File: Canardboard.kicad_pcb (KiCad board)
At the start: 4 copper layers, 56.1 x 68.5 mm, 143 parts, among them IC1 SIC437DED-T1-GE3, J1 RBUS, J2 USB_C_Receptacle_USB2.0, J3 Micro_SD_Card_Det, J4 Conn_01x02_Male, J5 Conn_01x03_Male, J6 Conn_01x03_Male, J7 Conn_01x03_Male, Q1 PXP012-30QLJ, Q10 PXP012-30QLJ, Q2 PXP012-30QLJ, Q3 PXP012-30QLJ, Q4 PXP012-30QLJ, Q5 PXP012-30QLJ, Q6 PXP012-30QLJ, Q7 PXP012-30QLJ, Q8 PXP012-30QLJ, Q9 PXP012-30QLJ, U1 ESP32-S3, U10 MP28167GQ-A-Z, U11 LTC4412xS6, U12 LTC4412xS6, U2 SN65HVD230, U3 LTC4412xS6, U4 LTC4412xS6, U5 LTC4412xS6, U7 ICM-20608-G, U8 MMC5983MA, Y1 40MHz±10ppm

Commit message: I don't want to lose all my changes so I will commit, commit.
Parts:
- removed C20: 390uF, Capacitor_SMD:CP_Elec_8x11.9
- removed C47: 100uF, Capacitor_SMD:CP_Elec_6.3x5.4
- removed Q10, Q3, Q5, Q7, Q8, Q9: PXP012-30QLJ, iclr:PXP01230QLJ
- removed U11, U12, U5: LTC4412xS6, Package_TO_SOT_SMD:TSOT-23-6
- added C18: 47uF, Capacitor_SMD:C_1206_3216Metric, F.Cu at (104.4, 84.1)
- added C19: 47uF, Capacitor_SMD:C_1206_3216Metric, F.Cu at (104.4, 81.6)
- added D3: D_Schottky, Diode_SMD:D_SOD-323, F.Cu at (109.0, 100.8)
- added D4: D_Schottky, Diode_SMD:D_SOD-323, F.Cu at (104.5, 122.9)
- added D5: D_Schottky, Diode_SMD:D_SOD-323, F.Cu at (110.6, 90.5)
- added R14: 10k, Resistor_SMD:R_0402_1005Metric, F.Cu at (128.5, 92.2)
- added TP10: TestPoint, TestPoint:TestPoint_Pad_D1.0mm, F.Cu at (122.8, 90.4)
- added TP11: TestPoint, TestPoint:TestPoint_Pad_D1.0mm, F.Cu at (126.0, 90.0)
- added TP12: TestPoint, TestPoint:TestPoint_Pad_D1.0mm, F.Cu at (128.1, 90.0)
- added TP13: TestPoint, TestPoint:TestPoint_Pad_D1.0mm, F.Cu at (130.2, 90.2)
- added TP14: TestPoint, TestPoint:TestPoint_Pad_D1.0mm, F.Cu at (114.1, 101.5)
- added TP15: TestPoint, TestPoint:TestPoint_Pad_D1.0mm, F.Cu at (114.1, 103.8)
- added TP5: TestPoint, TestPoint:TestPoint_Pad_D1.0mm, F.Cu at (116.7, 98.1)
- added TP6: TestPoint, TestPoint:TestPoint_Pad_D1.0mm, F.Cu at (118.2, 90.7)
- added TP7: TestPoint, TestPoint:TestPoint_Pad_D1.0mm, F.Cu at (115.4, 94.3)
- added TP8: TestPoint, TestPoint:TestPoint_Pad_D1.0mm, F.Cu at (117.1, 95.1)
- added TP9: TestPoint, TestPoint:TestPoint_Pad_D1.0mm, F.Cu at (113.5, 94.3)
- L4: footprint iclr:INDPM112100X400N -> iclr:INDPM3030X200N
- moved TP3 68.6 mm to (106.1, 79.0)
- moved 12VLED1 55.1 mm to (137.8, 145.9)
- moved R7 52.3 mm to (136.3, 145.7)
- moved TP2 45.2 mm to (119.5, 91.9)
- moved CANRXLED1 44.1 mm to (132.7, 129.5), turned to 180 degrees
- moved R10 43.0 mm to (123.7, 128.3)
- moved TP1 42.6 mm to (120.7, 90.4)
- moved R27 42.5 mm to (130.8, 129.5), turned to 0 degrees
- moved L5 42.4 mm to (111.9, 76.3), turned to 0 degrees
- moved C19 40.8 mm to (123.1, 127.1)
- moved C30 39.6 mm to (112.3, 99.5), turned to -90 degrees
- moved C33 38.8 mm to (113.2, 99.5), turned to -90 degrees
- moved J1 38.7 mm to (119.0, 127.4), turned to 180 degrees
- moved USBLED1 38.5 mm to (111.5, 97.4), turned to -90 degrees
- moved C17 38.2 mm to (125.0, 127.1), turned to 180 degrees
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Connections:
- BOOTJUMPER1 pad 1: unconnected-(BOOTJUMPER1-Pin_1-Pad1) -> GND
- C31 pad 1: Net-(U7-VDD) -> +3V3
- C33 pad 1: Net-(U7-VDD) -> +3V3
- C34 pad 1: Net-(U7-VDD) -> +3V3
- IC1 pad 29: unconnected-(IC1-PGND__5-Pad29) -> GND
- J1 pad 3: VBUS -> /rbusmosfets/RBUS_3.3
- J3 pad 10: +3V3 -> /SD_DET
- J3 pad 3: /SPI_MOSI -> /SD_MOSI
- J3 pad 5: /SPI_CLK -> /SD_CLK
- J3 pad 7: /SPI_MISO -> /SD_MISO
- Q1 pad 5: Net-(Q1-D_1) -> +12V
- Q1 pad 6: Net-(Q1-D_1) -> +12V
- Q1 pad 7: Net-(Q1-D_1) -> +12V
- Q1 pad 8: Net-(Q1-D_1) -> +12V
- Q1 pad 9: Net-(Q1-D_1) -> +12V
- Q2 pad 1: +12V -> Net-(Q1-S_1)
- Q2 pad 2: +12V -> Net-(Q1-S_1)
- Q2 pad 3: +12V -> Net-(Q1-S_1)
- Q2 pad 5: Net-(Q1-D_1) -> /rbusmosfets/RBUS_DEPL
- Q2 pad 6: Net-(Q1-D_1) -> /rbusmosfets/RBUS_DEPL
- Q2 pad 7: Net-(Q1-D_1) -> /rbusmosfets/RBUS_DEPL
- Q2 pad 8: Net-(Q1-D_1) -> /rbusmosfets/RBUS_DEPL
- Q2 pad 9: Net-(Q1-D_1) -> /rbusmosfets/RBUS_DEPL
- Q4 pad 1: /rbusmosfets/BatteryPower -> Net-(Q4-S_1)
- Q4 pad 2: /rbusmosfets/BatteryPower -> Net-(Q4-S_1)
- Q4 pad 3: /rbusmosfets/BatteryPower -> Net-(Q4-S_1)
- Q4 pad 5: Net-(Q4-D_1) -> +12V
- Q4 pad 6: Net-(Q4-D_1) -> +12V
- Q4 pad 7: Net-(Q4-D_1) -> +12V
- Q4 pad 8: Net-(Q4-D_1) -> +12V
- Q4 pad 9: Net-(Q4-D_1) -> +12V
- Q6 pad 1: +12V -> Net-(Q4-S_1)
- Q6 pad 2: +12V -> Net-(Q4-S_1)
- Q6 pad 3: +12V -> Net-(Q4-S_1)
- Q6 pad 5: Net-(Q4-D_1) -> /rbusmosfets/BatteryPower
- Q6 pad 6: Net-(Q4-D_1) -> /rbusmosfets/BatteryPower
- Q6 pad 7: Net-(Q4-D_1) -> /rbusmosfets/BatteryPower
- Q6 pad 8: Net-(Q4-D_1) -> /rbusmosfets/BatteryPower
- Q6 pad 9: Net-(Q4-D_1) -> /rbusmosfets/BatteryPower
- U1 pad 19: unconnected-(U1-GPIO14/ADC2_CH3-Pad19) -> /SD_DET
- U1 pad 21: unconnected-(U1-GPIO15/ADC2_CH4/XTAL_32K_P-Pad21) -> /SD_MISO
- U1 pad 22: unconnected-(U1-GPIO16/ADC2_CH5/XTAL_32K_N-Pad22) -> /SD_CLK
- U1 pad 23: unconnected-(U1-GPIO17/ADC2_CH6/DAC_2-Pad23) -> /SD_MOSI
- U1 pad 24: unconnected-(U1-GPIO18/ADC2_CH7/DAC_1-Pad24) -> /SD_CS
- U1 pad 36: /CAN_TX -> /SPI_MISO
- U1 pad 37: /CAN_RX -> /MAG_CS
- U1 pad 38: /SD_CS -> /IMU_CS
- U1 pad 41: /SPI_MISO -> /CAN_TX
- U1 pad 42: /SERVO_SGNL2 -> /CAN_RX
- U1 pad 45: /IMU_CS -> /SERVO_SGNL2
- U1 pad 47: /MAG_CS -> unconnected-(U1-MTDI/JTAG/GPIO41-Pad47)
- U1 pad 50: unconnected-(U1-U0RXD/PROG/GPIO44-Pad50) -> /RXD
- U3 pad 1: Net-(Q1-S_1) -> /rbusmosfets/RBUS_DEPL
- U7 pad 1: Net-(U7-VDD) -> +3V3
- U7 pad 16: Net-(U7-VDD) -> +3V3
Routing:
- net RBUS_uC_V: track 0.00 -> 64.8 mm
- net GND: track 0.06 -> 48.6 mm, vias 27 -> 34
- net +3V3: track 9.69 -> 44.8 mm, vias 2 -> 8
- net /SD_DET: track 0.00 -> 24.7 mm
- net /Data+: track 0.00 -> 24.5 mm
- net /rbusmosfets/BatteryPower: track 7.48 -> 31.9 mm
- net /Data-: track 0.00 -> 22.9 mm
- net /CAN-: track 0.00 -> 21.4 mm
- net /CAN+: track 0.00 -> 20.8 mm
- net Net-(JP1-B): track 0.00 -> 19.6 mm
- net /rbusmosfets/RBUS_DEPL: track 0.00 -> 17.5 mm
- net VBUS: track 0.00 -> 15.9 mm
- net /SPI_MISO: track 0.00 -> 15.8 mm, vias 0 -> 3
- net Net-(Q1-G): track 0.00 -> 15.6 mm
- net /servopower/uC_VCC: track 0.00 -> 14.8 mm, vias 0 -> 2
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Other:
- board size 56.1 x 68.5 mm -> 42.3 x 58.8 mm

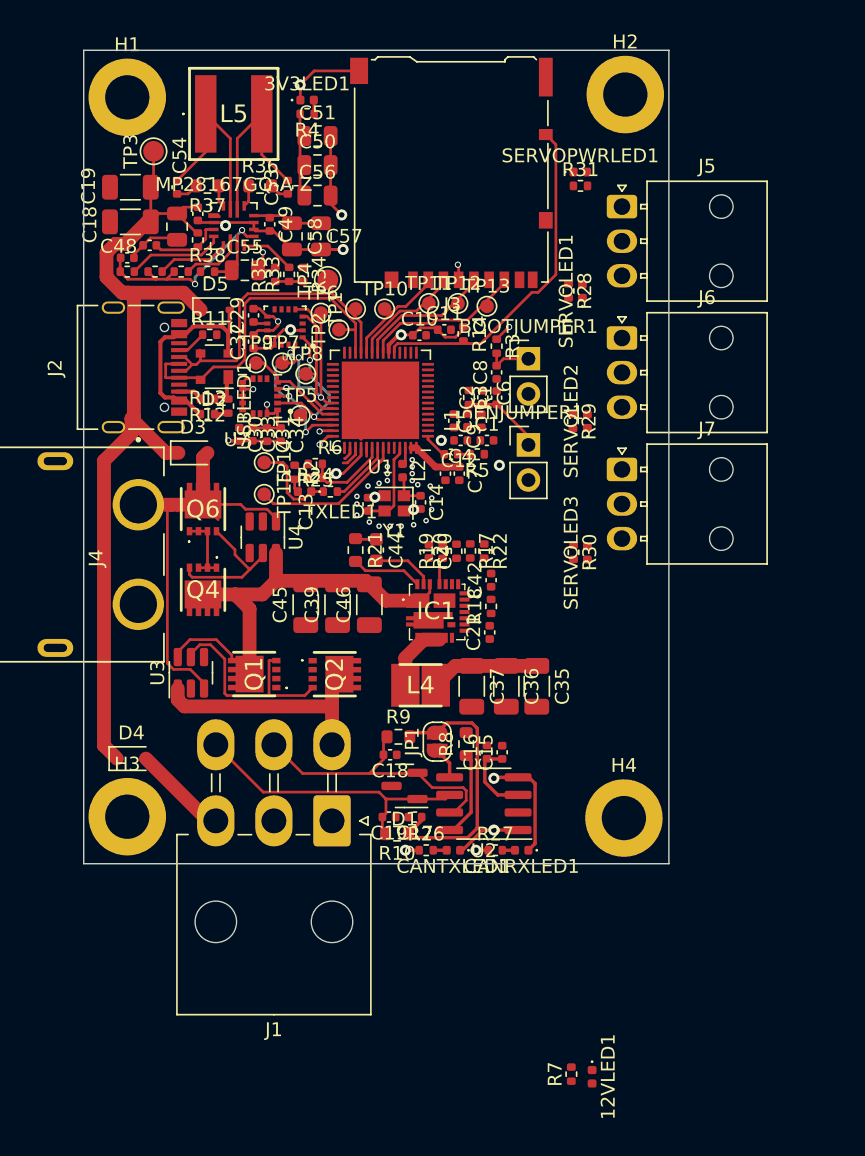
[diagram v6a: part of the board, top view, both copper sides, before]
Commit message: First PCB layout draft
I need to learn how to properly do fills
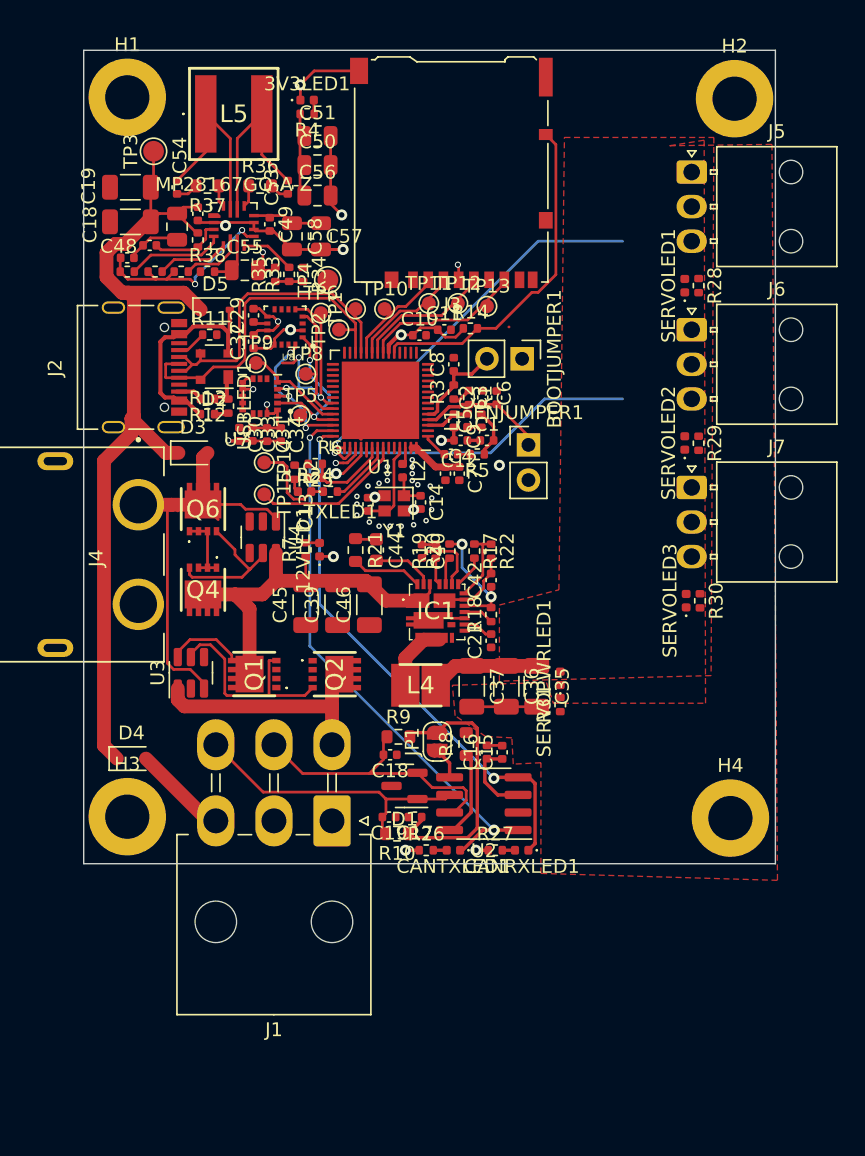
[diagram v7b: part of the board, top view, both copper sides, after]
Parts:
- removed TP7: TestPoint, TestPoint:TestPoint_Pad_D1.0mm
- moved 12VLED1 42.9 mm to (118.1, 107.8), turned to 90 degrees
- moved R7 42.5 mm to (117.1, 107.8)
- moved R31 37.5 mm to (135.5, 119.0), turned to 90 degrees
- moved SERVOPWRLED1 36.6 mm to (135.5, 117.1), turned to 90 degrees
- moved R30 9.79 mm to (145.6, 111.5)
- moved R28 9.41 mm to (145.5, 88.7)
- moved R29 9.22 mm to (145.5, 100.1)
- moved SERVOLED3 7.93 mm to (144.6, 111.5)
- moved H2 7.91 mm to (148.1, 75.2)
- moved H4 7.70 mm to (147.8, 127.2)
- moved SERVOLED1 7.41 mm to (144.5, 88.7)
- moved SERVOLED2 7.21 mm to (144.5, 100.1)
- moved J5 5.63 mm to (145.0, 80.5)
- moved J7 5.20 mm to (145.0, 103.3)
- moved J6 5.08 mm to (145.0, 91.9)
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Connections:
- U1 pad 44: /SERVO_SGNL3 -> /SERVO_SGNL2
- U1 pad 45: /SERVO_SGNL2 -> /SERVO_SGNL3
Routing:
- net /CAN_TX: track 5.78 -> 40.5 mm
- net /CAN_RX: track 9.50 -> 39.0 mm
- net /SERVO_SGNL1: track 0.00 -> 27.7 mm, vias 0 -> 1
- net /SERVO_SGNL2: track 1.64 -> 24.3 mm, vias 0 -> 1
- net GND: track 48.6 -> 62.5 mm, vias 34 -> 35
- net /servopower/VDD: track 0.00 -> 9.13 mm, vias 0 -> 2
- net +12V: track 31.9 -> 39.1 mm
- net GNDA: track 0.00 -> 6.61 mm
- net Net-(IC1-FB): track 0.00 -> 5.33 mm
- net /CHIP_PU: track 5.90 -> 9.31 mm
- net /BOOT: track 3.41 -> 6.80 mm
- net Net-(C6-Pad1): track 0.00 -> 3.21 mm
- net /SERVO_PWR: track 7.88 -> 10.2 mm
- net Net-(IC1-VDRV): track 0.00 -> 2.21 mm
- net /servopower/PGOOD: track 0.00 -> 2.21 mm
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- added copper zone on F.Cu, net /SERVO_PWR
- added copper zone on F.Cu, net GND
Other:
- board size 42.3 x 58.8 mm -> 50 x 58.8 mm

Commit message: i dont know
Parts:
- added TP7: TestPoint, TestPoint:TestPoint_Pad_D1.0mm, F.Cu at (1.02, 1.02)
- L4: footprint iclr:INDPM3030X200N -> iclr:INDPM112100X400N
- moved R31 16.9 mm to (138.4, 102.3), turned to 0 degrees
- moved SERVOPWRLED1 15.6 mm to (140.3, 102.3), turned to 0 degrees
- moved L4 15.0 mm to (138.2, 109.7), turned to -90 degrees
- moved C45 14.0 mm to (129.2, 118.7), turned to 180 degrees
- moved C39 10.9 mm to (129.2, 116.4), turned to 180 degrees
- moved C37 9.87 mm to (138.9, 118.8), turned to 90 degrees
- moved TP6 9.63 mm to (115.7, 100.0)
- moved C21 9.42 mm to (132.2, 105.1), turned to -90 degrees
- moved C46 7.88 mm to (129.2, 114.1), turned to 180 degrees
- moved R18 7.41 mm to (131.2, 105.1)
- moved C42 6.36 mm to (129.6, 103.7), turned to 180 degrees
- moved C36 4.94 mm to (136.4, 118.8), turned to 90 degrees
- moved IC1 4.41 mm to (130.0, 109.5), turned to 90 degrees
- moved R22 3.62 mm to (128.2, 105.1), turned to 90 degrees
- moved R17 3.41 mm to (127.2, 105.2), turned to 90 degrees
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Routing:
- net /SERVO_SGNL3: track 2.17 -> 36.0 mm
- net +12V: track 39.1 -> 19.4 mm
- net GNDA: track 6.61 -> 23.3 mm, vias 0 -> 2
- net /SERVO_SGNL1: track 27.7 -> 35.6 mm
- net /SERVO_SGNL2: track 24.3 -> 32.2 mm
- net /servopower/PGOOD: track 2.21 -> 9.60 mm, vias 0 -> 3
- net GND: track 62.5 -> 69.7 mm, vias 35 -> 32
- net /SERVO_PWR: track 10.2 -> 15.6 mm, vias 0 -> 2
- net /servopower/SW: track 4.99 -> 0.00 mm
- net /BOOT: track 6.80 -> 10.3 mm
- net Net-(U7-REGOUT): track 0.00 -> 2.56 mm
- net Net-(IC1-FB): track 5.33 -> 3.17 mm
- net /SPI_MOSI: track 10.9 -> 12.7 mm
- net Net-(C44-Pad1): track 1.52 -> 0.00 mm
- net Net-(IC1-MODE2): track 2.00 -> 3.36 mm
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- added copper zone on F.Cu, net +12V
- added copper zone on F.Cu, net /servopower/SW
